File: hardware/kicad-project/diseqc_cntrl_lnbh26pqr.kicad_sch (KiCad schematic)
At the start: 23 parts, among them IC5 LNBH26PQR, J6 SMA_Sock, J7 SMA_Sock

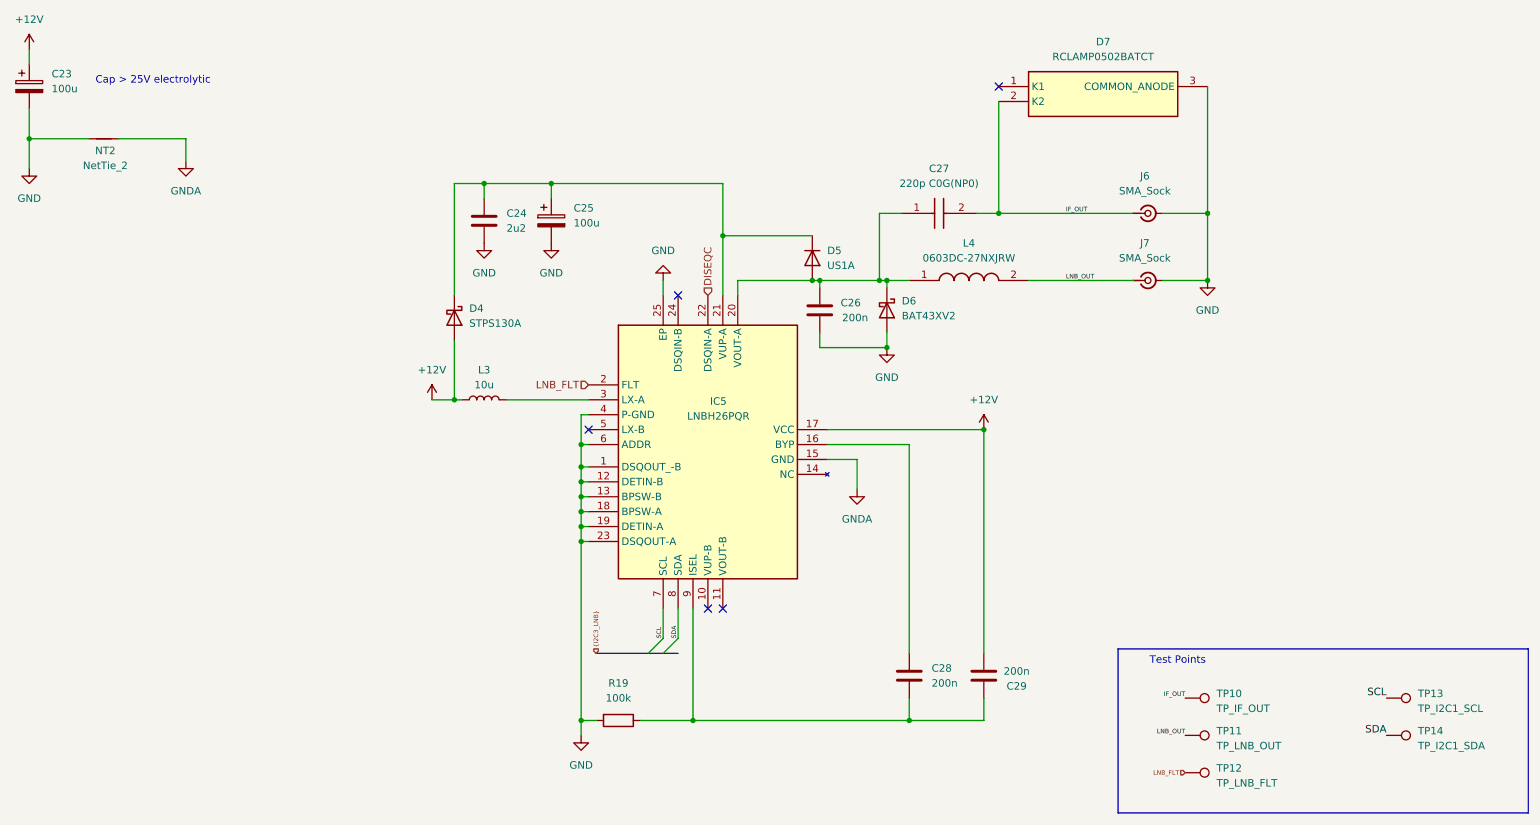
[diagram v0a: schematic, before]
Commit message: Placed LNBH26
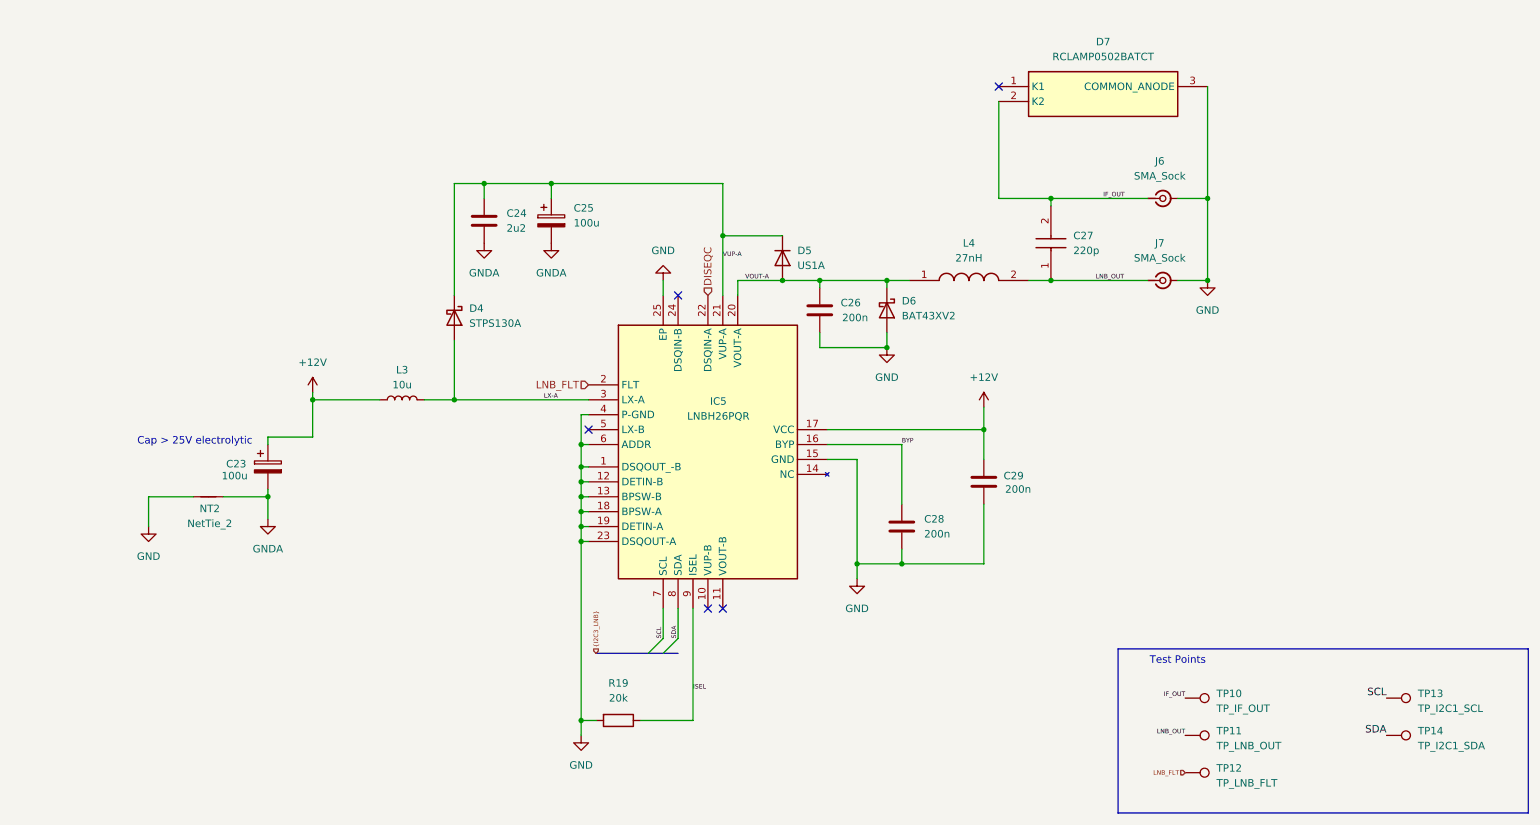
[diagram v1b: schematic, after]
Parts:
- C27: value 220p C0G(NP0) -> 220p
- L4: value 0603DC-27NXJRW -> 27nH
- R19: value 100k -> 20k; symbol diseqc_cntrl:R -> #InvenTree:R_20k_0603_1%; InvenTree 105 -> 118; InvenTree Part R_100k_0603 -> R_20k_0603; Part URL (none) -> https://inventree.ebnx.net/web/part/118/; Tolerance (none) -> 1%
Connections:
- net +12V: no longer D4.2 (A)
- net GND: now also C28.1, C29.1, IC5.15 (GND); no longer C23.2, C24.2, C25.2
- net GNDA: now also C23.2, C24.2, C25.2; no longer IC5.15 (GND)
- net LNB_OUT: now also C27.1
- net VOUT-A: now reaches C26.1, D5.2 (A), D6.1 (K), IC5.20 (VOUT-A), L4.1
- net VOUT-A: no longer C27.1
- net BYP: now reaches C28.2, IC5.16 (BYP)
- net VUP-A: now reaches C24.1, C25.1, D4.1 (K), D5.1 (K), IC5.21 (VUP-A)
- net LX-A: now reaches IC5.3 (LX-A), L3.2
- net LX-A: now also D4.2 (A)
- net ISEL: now reaches IC5.9 (ISEL), R19.1
- net ISEL: no longer C28.1, C29.1
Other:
- moved on the sheet: C27, C28, C29, D5, J6, J7, L3

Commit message: Adding test points
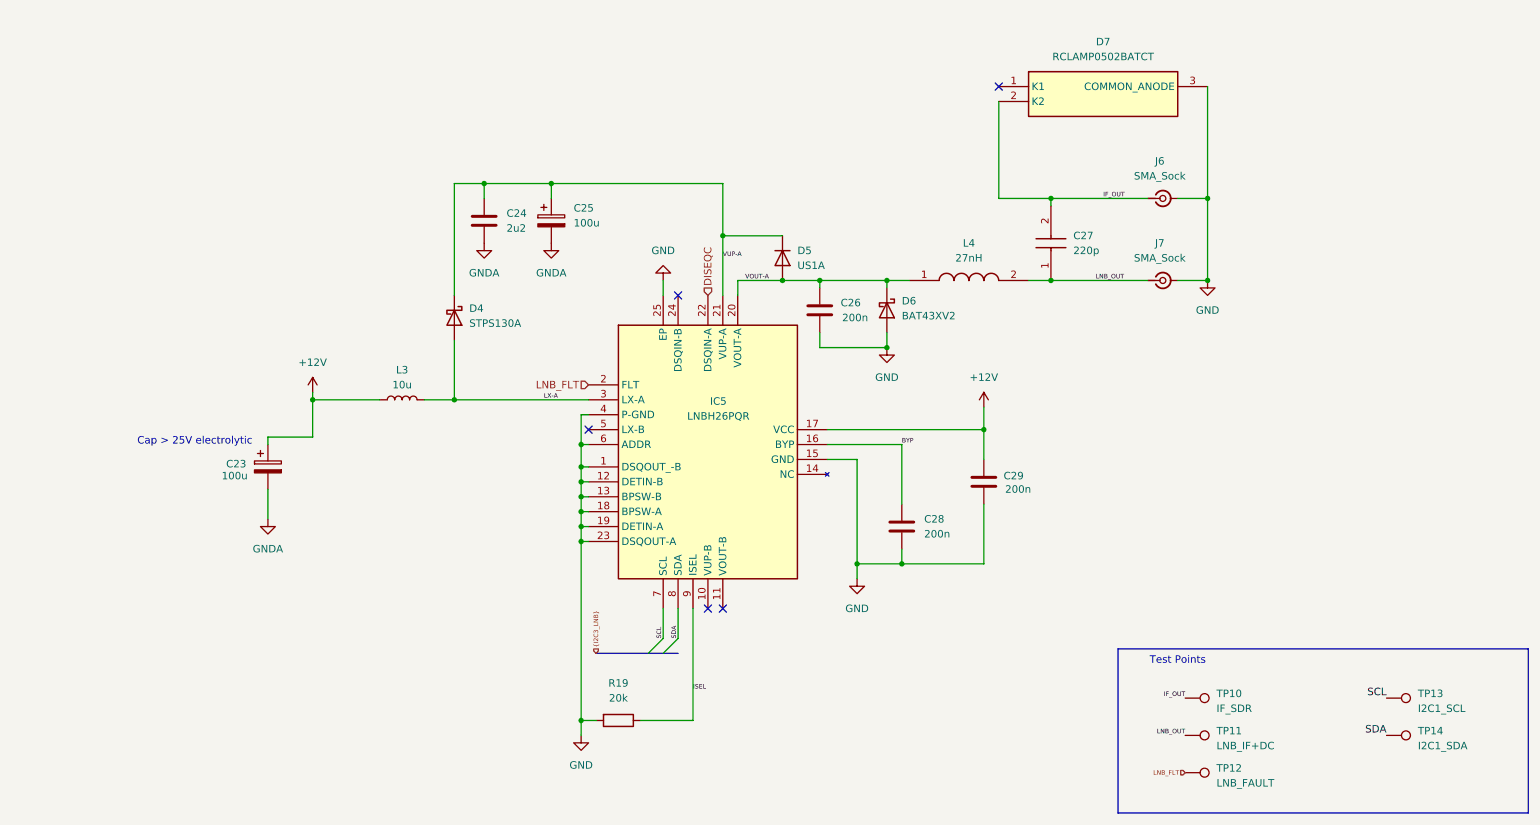
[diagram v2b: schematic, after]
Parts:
- removed NT2: NetTie_2, NetTie:NetTie-2_SMD_Pad2.0mm, symbol diseqc_cntrl:NetTie_2
- TP10: value TP_IF_OUT -> IF_SDR; footprint TestPoint:TestPoint_THTPad_D1.0mm_Drill0.5mm -> ebnx_footprints:TestPoint_THTPad_D1.0mm_Drill0.5mm_annotated; symbol Connector:TestPoint -> ebnx_symbols:TestPoint_Annotated_Silkscreen; now in the parts list
- TP11: value TP_LNB_OUT -> LNB_IF+DC; footprint TestPoint:TestPoint_THTPad_D1.0mm_Drill0.5mm -> ebnx_footprints:TestPoint_THTPad_D1.0mm_Drill0.5mm_annotated; symbol Connector:TestPoint -> ebnx_symbols:TestPoint_Annotated_Silkscreen; now in the parts list
- TP12: value TP_LNB_FLT -> LNB_FAULT; footprint TestPoint:TestPoint_THTPad_D1.0mm_Drill0.5mm -> ebnx_footprints:TestPoint_THTPad_D1.0mm_Drill0.5mm_annotated; symbol Connector:TestPoint -> ebnx_symbols:TestPoint_Annotated_Silkscreen; now in the parts list
- TP13: value TP_I2C1_SCL -> I2C1_SCL; footprint TestPoint:TestPoint_THTPad_D1.0mm_Drill0.5mm -> ebnx_footprints:TestPoint_THTPad_D1.0mm_Drill0.5mm_annotated; symbol Connector:TestPoint -> ebnx_symbols:TestPoint_Annotated_Silkscreen; now in the parts list
- TP14: value TP_I2C1_SDA -> I2C1_SDA; footprint TestPoint:TestPoint_THTPad_D1.0mm_Drill0.5mm -> ebnx_footprints:TestPoint_THTPad_D1.0mm_Drill0.5mm_annotated; symbol Connector:TestPoint -> ebnx_symbols:TestPoint_Annotated_Silkscreen; now in the parts list

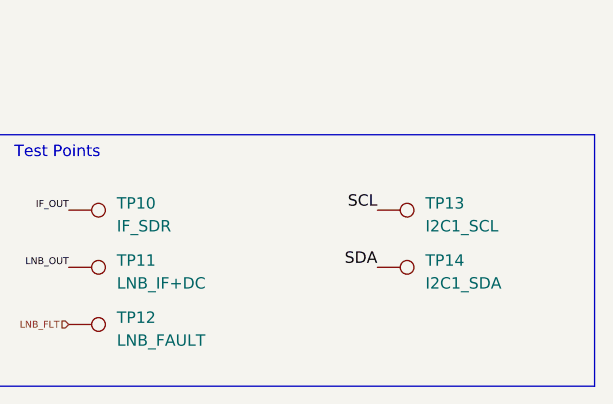
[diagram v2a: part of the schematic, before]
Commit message: v0.5 routing complete
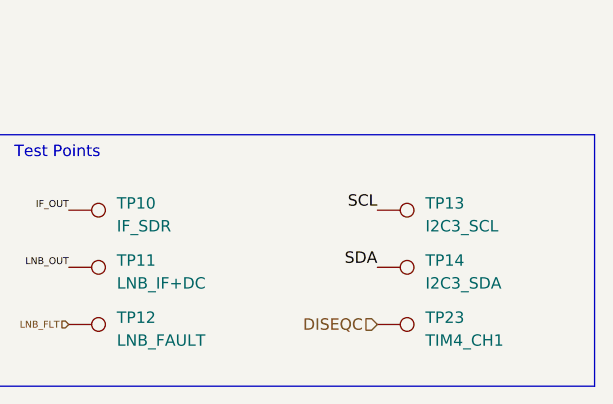
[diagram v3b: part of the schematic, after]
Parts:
- added TP23: TIM4_CH1, ebnx_footprints:TestPoint_THTPad_D1.0mm_Drill0.5mm_annotated, symbol ebnx_symbols:TestPoint_Annotated_Silkscreen
- TP13: value I2C1_SCL -> I2C3_SCL
- TP14: value I2C1_SDA -> I2C3_SDA
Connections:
- net DISEQC: now also TP23.1
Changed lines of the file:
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@@
 	(hierarchical_label "DISEQC"
 		(shape input)
+		(at 256.54 151.13 180)
+		(effects
+			(font
+				(size 1.27 1.27)
+			)
+			(justify right)
+		)
+	)
+	(hierarchical_label "DISEQC"
+		(shape input)
 		(at 140.97 69.85 90)
 		(effects
@@
 			)
 		)
-		(property "Value" "I2C1_SCL"
+		(property "Value" "I2C3_SCL"
 			(at 261.874 140.208 90)
 			(show_name no)
@@
 	)
 	(symbol
+		(lib_id "ebnx_symbols:TestPoint_Annotated_Silkscreen")
+		(at 256.54 151.13 270)
+		(unit 1)
+		(body_style 1)
+		(exclude_from_sim no)
+		(in_bom yes)
+		(on_board yes)
+		(in_pos_files yes)
+		(dnp no)
+		(property "Reference" "TP23"
+			(at 261.874 150.368 90)
+			(show_name no)
+			(do_not_autoplace no)
+			(effects
+				(font
+					(size 1.27 1.27)
+				)
+				(justify left)
+			)
+		)
+		(property "Value" "TIM4_CH1"
+			(at 261.874 152.908 90)
+			(show_name no)
+			(do_not_autoplace no)
+			(effects
+				(font
+					(size 1.27 1.27)
+				)
+				(justify left)
+			)
+		)
+		(property "Footprint" "ebnx_footprints:TestPoint_THTPad_D1.0mm_Drill0.5mm_annotated"
+			(at 256.54 156.21 0)
+			(hide yes)
+			(show_name no)
+			(do_not_autoplace no)
+			(effects
+				(font
+					(size 1.27 1.27)
+				)
+			)
+		)
+		(property "Datasheet" ""
+			(at 256.54 156.21 0)
+			(hide yes)
+			(show_name no)
+			(do_not_autoplace no)
+			(effects
+				(font
+					(size 1.27 1.27)
+				)
+			)
+		)
+		(property "Description" "test point"
+			(at 256.54 151.13 0)
+			(hide yes)
+			(show_name no)
+			(do_not_autoplace no)
+			(effects
+				(font
+					(size 1.27 1.27)
+				)
+			)
+		)
+		(property "InvenTree Part" ""
+			(at 256.54 151.13 90)
+			(hide yes)
+			(show_name no)
+			(do_not_autoplace no)
+			(effects
+				(font
+					(size 1.27 1.27)
+				)
+			)
+		)
+		(property "KLC_S4.2_3V3OUT" ""
+			(at 256.54 151.13 90)
+			(hide yes)
+			(show_name no)
+			(do_not_autoplace no)
+			(effects
+				(font
+					(size 1.27 1.27)
+				)
+			)
+		)
+		(property "KLC_S4.2_VCC" ""
+			(at 256.54 151.13 90)
+			(hide yes)
+			(show_name no)
+			(do_not_autoplace no)
+			(effects
+				(font
+					(size 1.27 1.27)
+				)
+			)
+		)
+		(property "Tolerance" ""
+			(at 256.54 151.13 90)
+			(hide yes)
+			(show_name no)
+			(do_not_autoplace no)
+			(effects
+				(font
+					(size 1.27 1.27)
+				)
+			)
+		)
+		(pin "1"
+		)
+		(instances
+			(project "diseqc_cntrl"
+				(path "/82a905d8-f1d7-4995-9c16-94cf3cdcaad9/65fcf1a0-d0f2-4bf0-9977-67dd9f84afa5/114baf94-7b4a-4d2d-92f4-f2fc3fb70423"
+					(reference "TP23")
+					(unit 1)
+				)
+			)
+		)
+	)
+	(symbol
 		(lib_id "diseqc_cntrl:GRM1885C2A221JA01D")
 		(at 199.39 67.31 90)
@@
 			)
 		)
-		(property "Value" "I2C1_SDA"
+		(property "Value" "I2C3_SDA"
 			(at 261.874 146.558 90)
 			(show_name no)
